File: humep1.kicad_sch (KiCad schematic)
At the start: 11 parts, among them U1 LM1117LD-3.3, U2 113991054

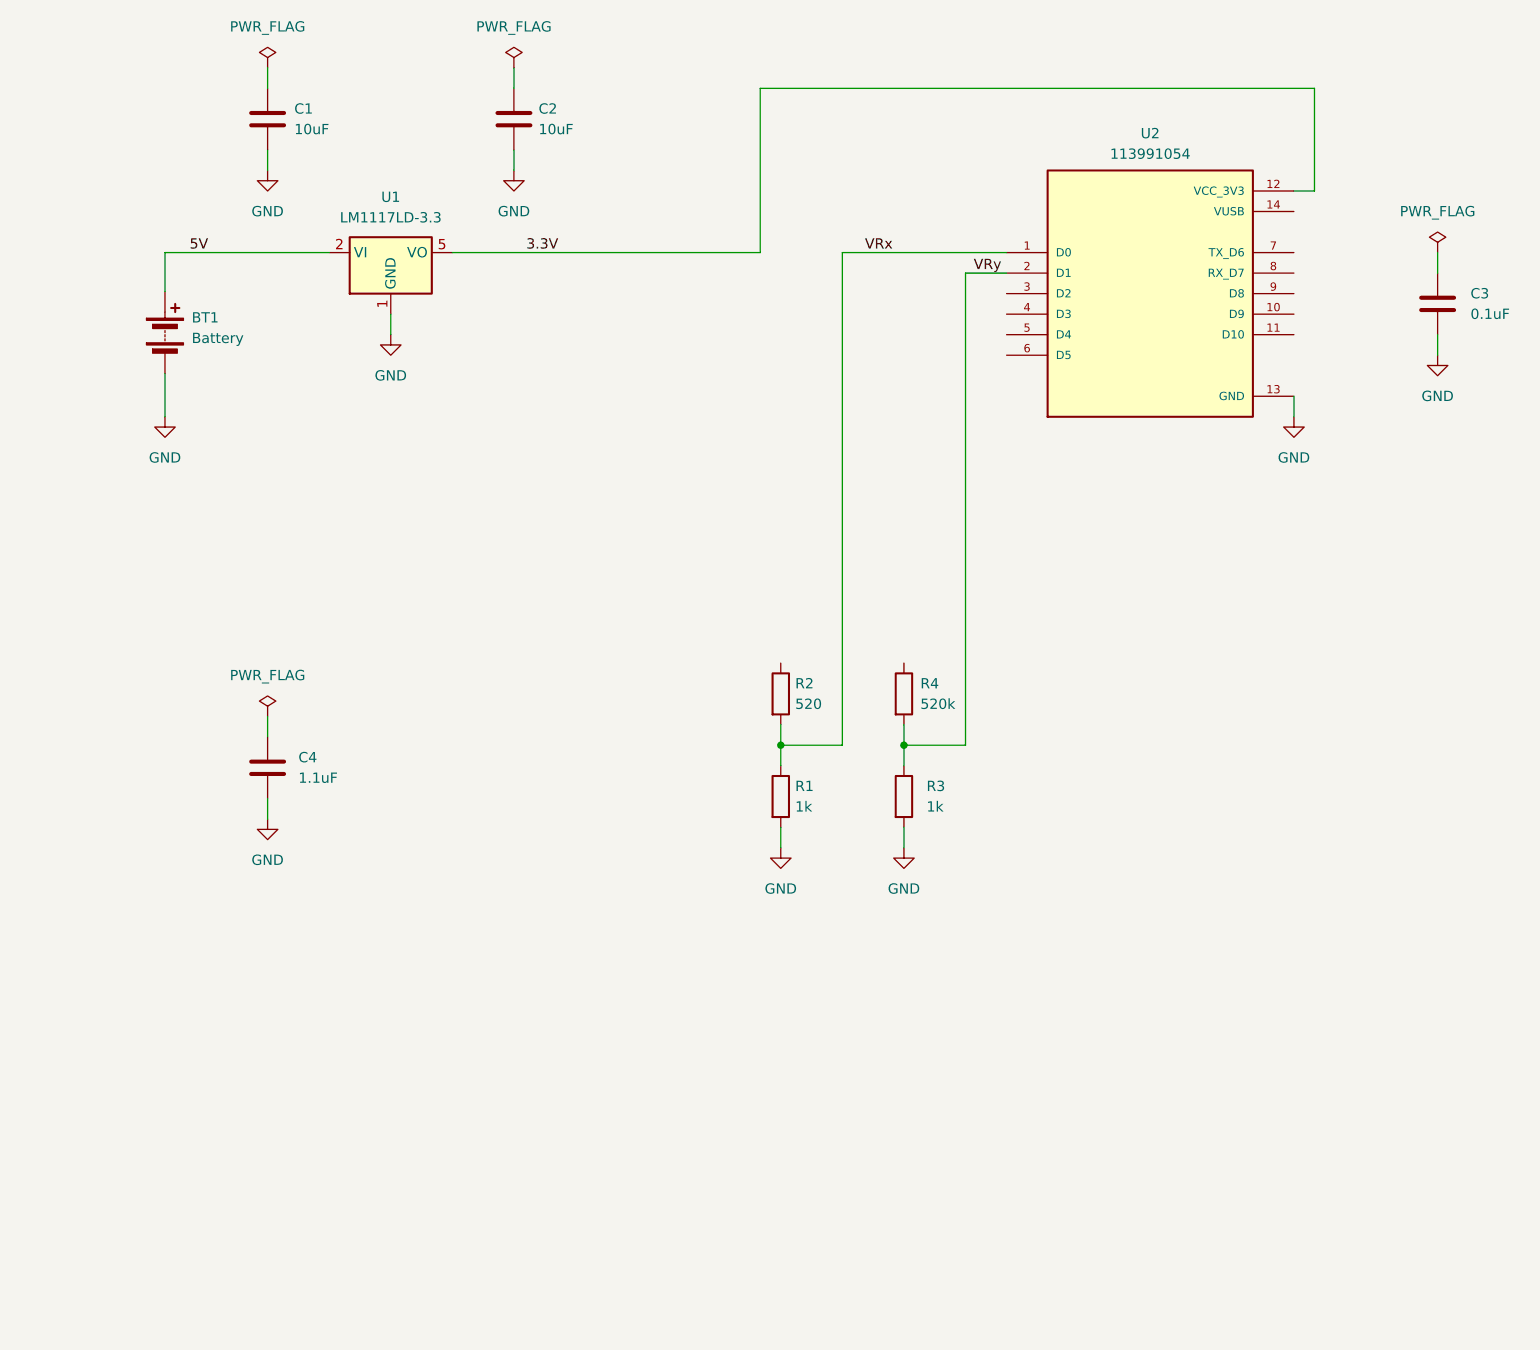
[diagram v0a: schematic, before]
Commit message: completed footprint assignments
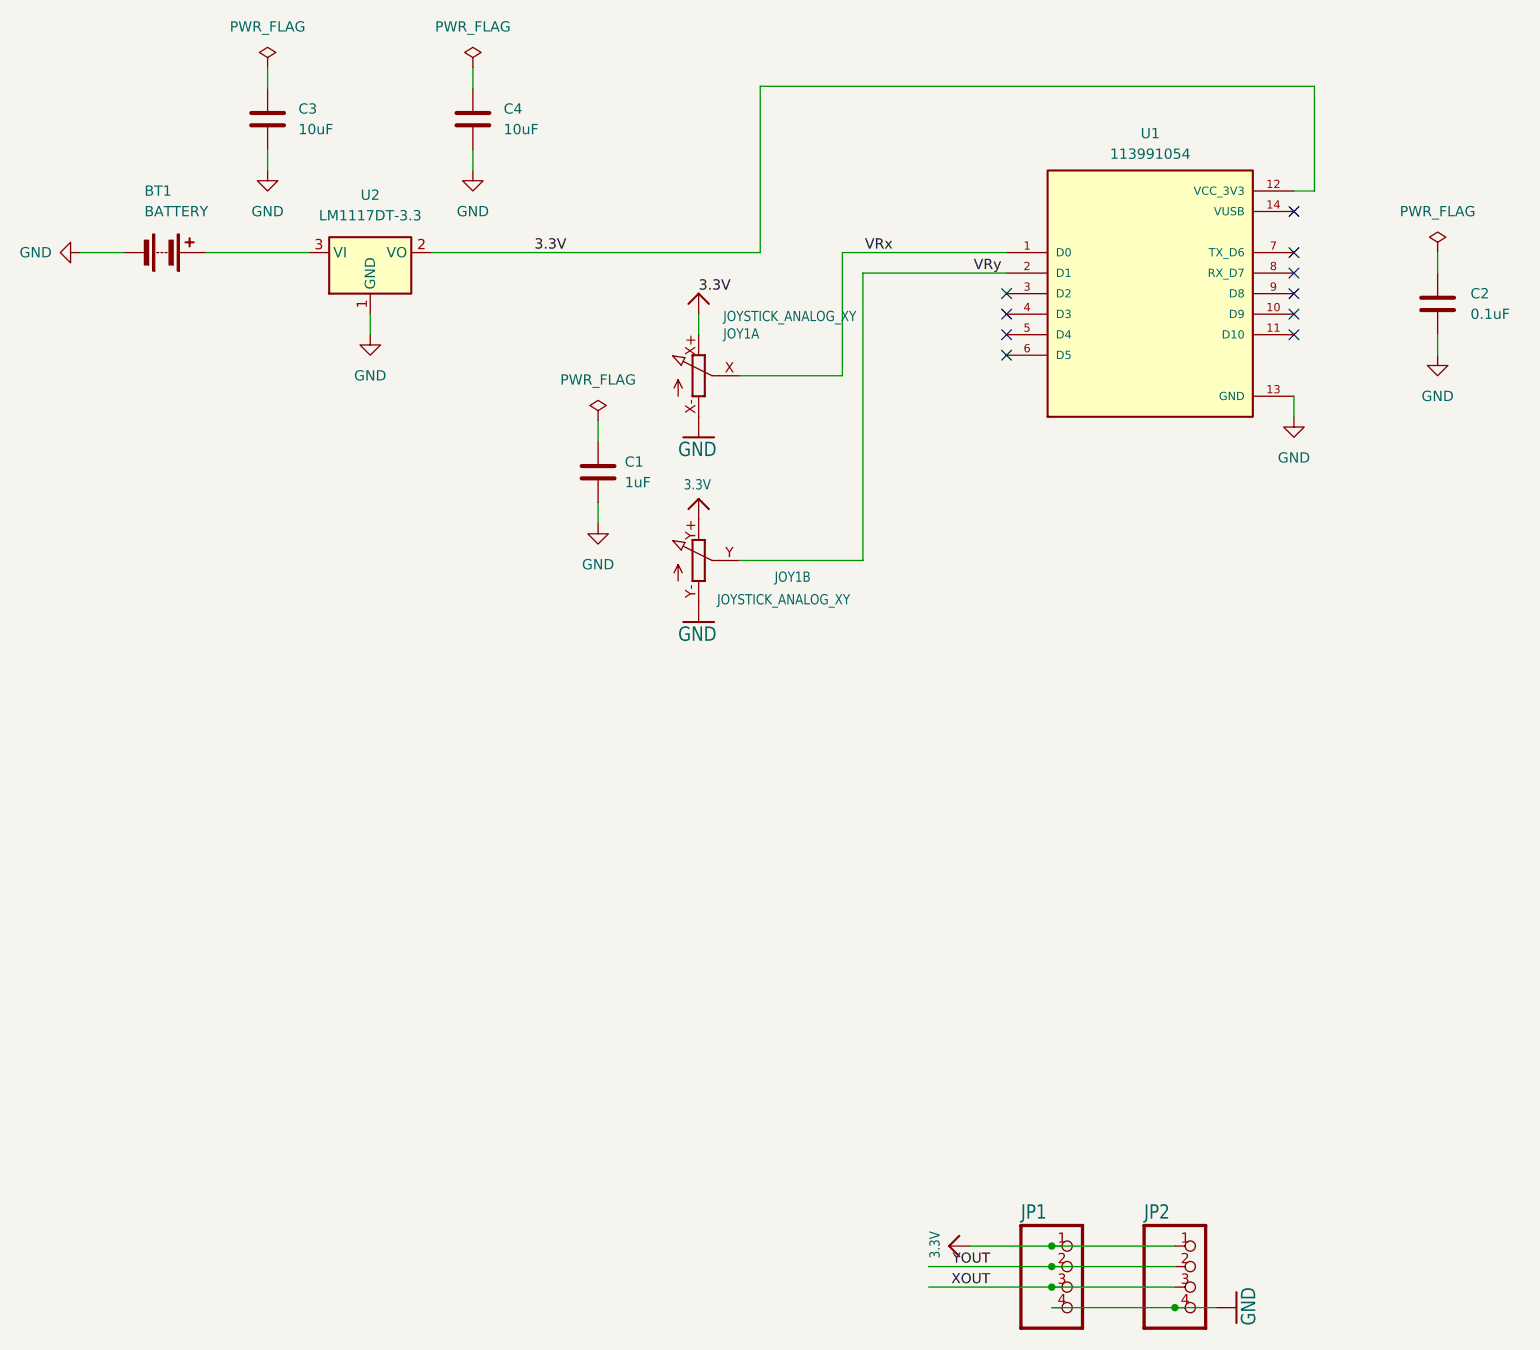
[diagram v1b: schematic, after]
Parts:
- removed C1, C2: 10uF, symbol Device:C
- removed R1, R3: 1k, symbol Device:R
- removed R2: 520, symbol Device:R
- removed R4: 520k, symbol Device:R
- removed U1: LM1117LD-3.3, Package_SON:WSON-8-1EP_4x4mm_P0.8mm_EP2.2x3mm, symbol Regulator_Linear:LM1117LD-3.3
- added C3, C4: 10uF, Capacitor_SMD:C_0805_2012Metric_Pad1.18x1.45mm_HandSolder, symbol Device:C
- added JOY1: JOYSTICK_ANALOG_XY, Adafruit Mini Analog Thumbstick:JOYSTICK_ANALOG_MINITHM, symbol Adafruit Mini Analog Thumbstick-eagle-import:microbuilder_JOYSTICK_ANALOG_XY
- added JP1, JP2: HEADER-1X476MIL, Adafruit Mini Analog Thumbstick:1X04_ROUND_76, symbol Adafruit Mini Analog Thumbstick-eagle-import:microbuilder_HEADER-1X476MIL
- added U2: LM1117DT-3.3, Package_TO_SOT_SMD:TO-252-3_TabPin2, symbol Regulator_Linear:LM1117DT-3.3
- BT1: value Battery -> BATTERY; footprint (none) -> Connector_Molex:Molex_PicoBlade_53398-0271_1x02-1MP_P1.25mm_Vertical
- C1: renamed from C4; value 1.1uF -> 1uF; footprint (none) -> Capacitor_SMD:C_0402_1005Metric_Pad0.74x0.62mm_HandSolder
- C2: renamed from C3; footprint (none) -> Capacitor_SMD:C_0603_1608Metric_Pad1.08x0.95mm_HandSolder
- renumbered U2 to U1
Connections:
- net 3.3V: now also JOY1.X+ (E), JOY1.Y+ (E), JP1.1, JP2.1, U2.2 (VO)
- net GND: now also C3.2, C4.2, JOY1.X- (A), JOY1.Y- (A), JP1.4, JP2.4, U2.1 (GND)
- net VRx: now also JOY1.X (S)
- net VRy: now also JOY1.Y (S)
- net 5V: no longer names the net of BT1.1 (+)
- net 5V: now also U2.3 (VI)
- new net XOUT: JP1.3, JP2.3
- new net YOUT: JP1.2, JP2.2
- no-connect marks 0 -> 10
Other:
- moved on the sheet: BT1, C1

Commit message: formatted pcb
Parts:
- removed C4: 10uF, Capacitor_SMD:C_0805_2012Metric_Pad1.18x1.45mm_HandSolder, symbol Device:C
- removed JOY1: JOYSTICK_ANALOG_XY, Adafruit Mini Analog Thumbstick:JOYSTICK_ANALOG_MINITHM, symbol Adafruit Mini Analog Thumbstick-eagle-import:microbuilder_JOYSTICK_ANALOG_XY
- removed JP1, JP2: HEADER-1X476MIL, Adafruit Mini Analog Thumbstick:1X04_ROUND_76, symbol Adafruit Mini Analog Thumbstick-eagle-import:microbuilder_HEADER-1X476MIL
- added C2: 10uF, Capacitor_SMD:C_0805_2012Metric_Pad1.18x1.45mm_HandSolder, symbol Device:C
- added JOY2: ~, Adafruit Mini Analog Thumbstick:JOYSTICK_ANALOG_MINITHM, symbol Adafruit Mini Analog Thumbstick-eagle-import:JOYSTICK_ANALOG_XY
- renumbered C3 to C1, C1 to C3, C2 to C4, U2 to U1, U1 to U2
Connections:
- net 3.3V: now also JOY2.X+ (E), JOY2.Y+ (E)
- net GND: now also C2.2, JOY2.X- (A), JOY2.Y- (A)
- net PWR: now reaches BT1.1 (+), U1.3 (VI)
- net PWR: now also C1.1, C3.1, C4.1, C2.1
- net VRx renamed X
- net X: now also JOY2.X (S)
- net VRy renamed Y
- net Y: now also JOY2.Y (S)
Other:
- moved on the sheet: C3

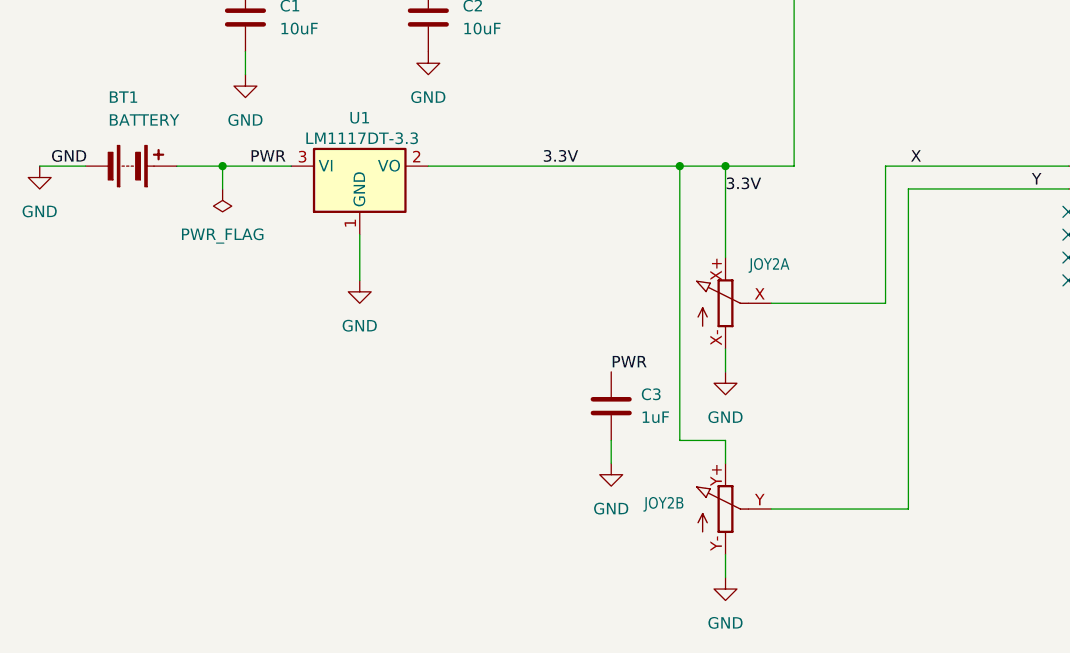
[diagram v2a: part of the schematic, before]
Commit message: updated schematic + completed pcb layout
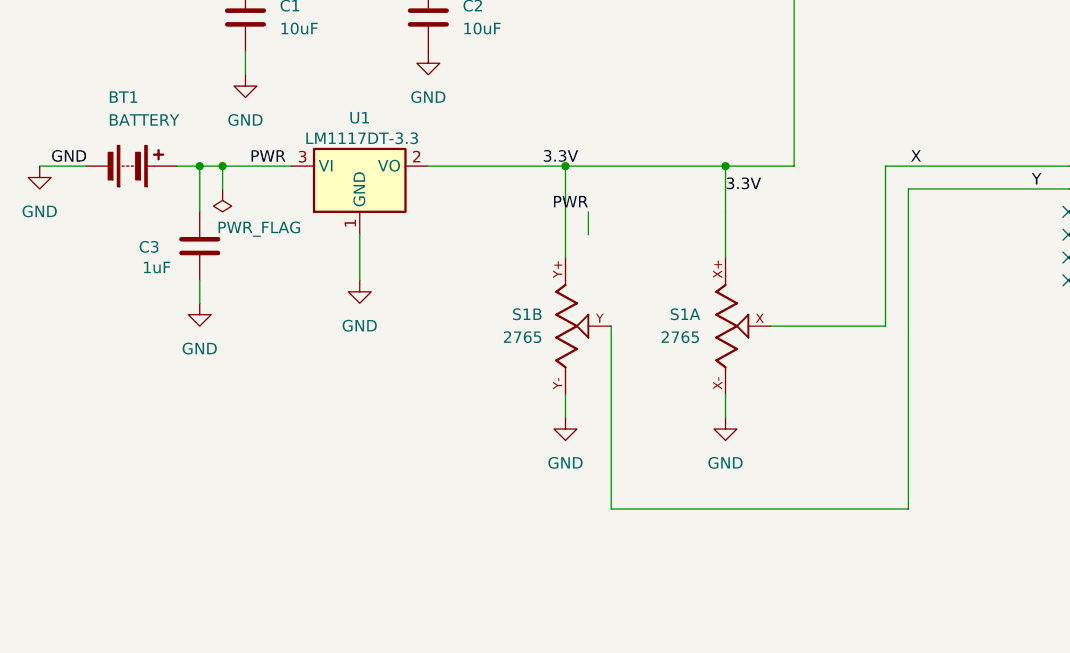
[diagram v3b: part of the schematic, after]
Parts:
- removed JOY2: ~, Adafruit Mini Analog Thumbstick:JOYSTICK_ANALOG_MINITHM, symbol Adafruit Mini Analog Thumbstick-eagle-import:JOYSTICK_ANALOG_XY
- added S1: 2765, 2765:SW_2765, symbol 2765:2765
- C3: footprint Capacitor_SMD:C_0402_1005Metric_Pad0.74x0.62mm_HandSolder -> Capacitor_SMD:C_0805_2012Metric_Pad1.18x1.45mm_HandSolder
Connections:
- net 3.3V: now also S1.X+, S1.Y+
- net GND: now also S1.X-, S1.Y-
- net X: now also S1.X
- net Y: now also S1.Y
